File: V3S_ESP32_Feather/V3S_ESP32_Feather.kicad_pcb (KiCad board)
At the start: 4 copper layers, 30.5 x 48.3 mm, 94 parts, among them J1 USB_B_Micro, J2 Bat, J3 CAM, J4 PWM, J5 U.FL-R-SMT(01), J6 UART, J7 Micro_SD_Card_Det, J8 I2C, J9 I2C, U1 V3S, U2 MIC5504-1.2YM5, U3 MIC5501-3.0YM5, U4 ICM-20948, U5 ESP32-PICO-D4, U6 LT1963AxST-3.3, U7 BMP280, U8 MIC5504-1.8YM5, U9 MAX13030EEBET, Y1 X1E0000210832, Y2 CC5V-T1A 32.768KHZ +-20PPM 12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

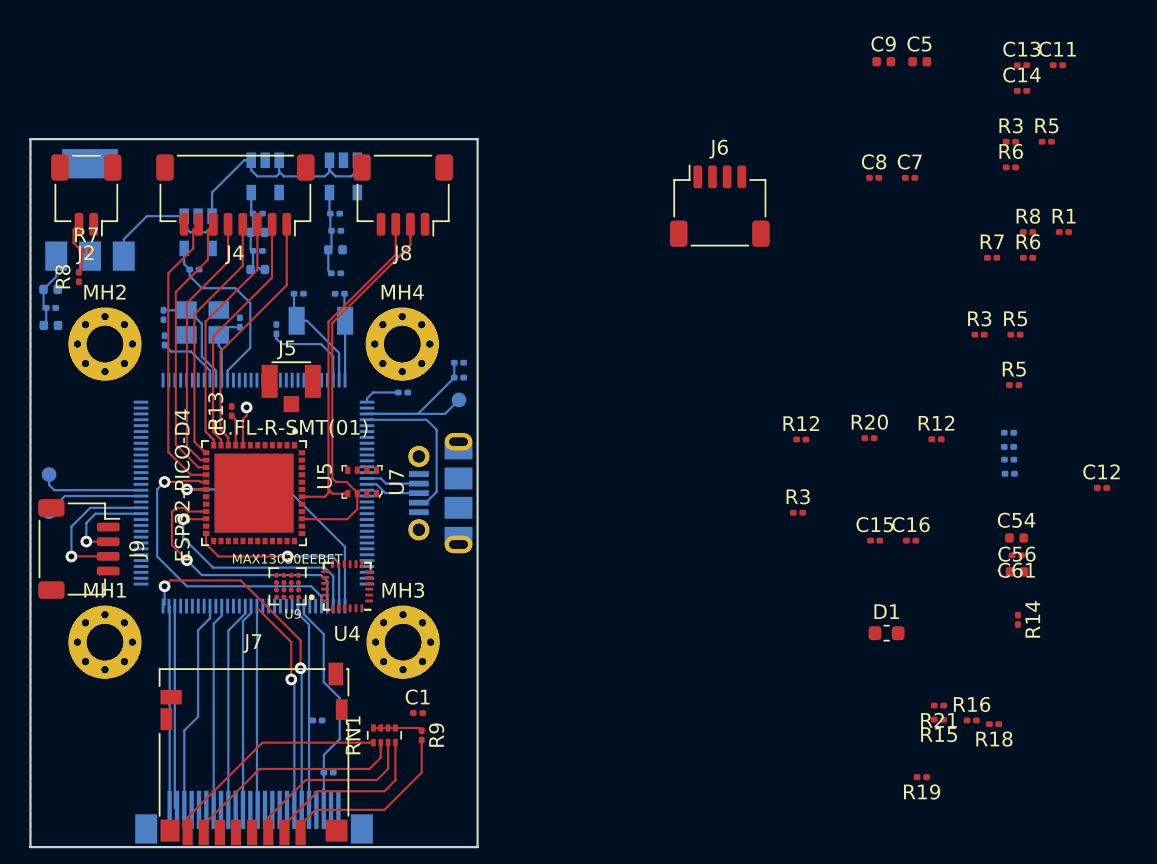
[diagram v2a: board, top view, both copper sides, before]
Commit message: Change Max13030 and moove ESP32
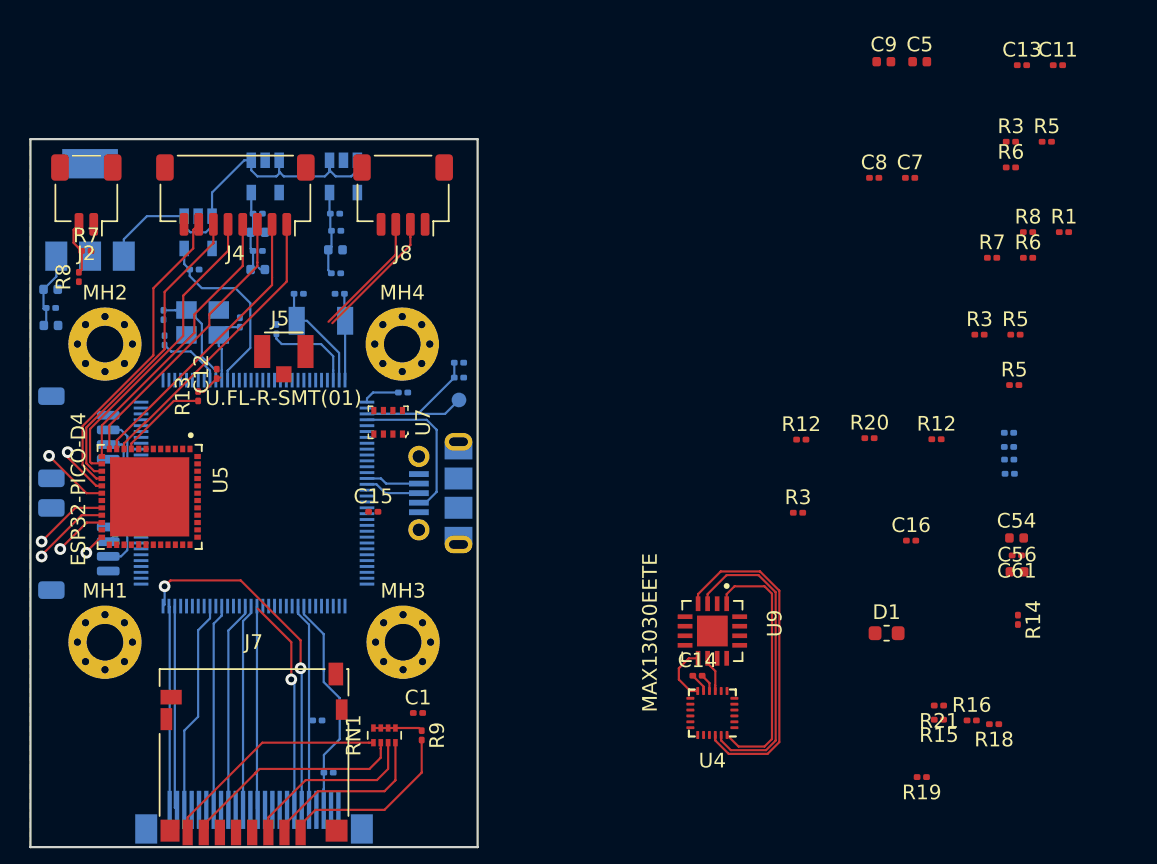
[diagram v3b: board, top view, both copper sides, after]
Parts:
- removed J6: UART, Connector_JST:JST_SH_SM04B-SRSS-TB_1x04-1MP_P1.00mm_Horizontal
- removed TP2: CPU_RX, TestPoint:TestPoint_Pad_D1.0mm
- removed TP3: CPU_TX, TestPoint:TestPoint_Pad_D1.0mm
- added J10: UART, Connector_JST:JST_SH_SM04B-SRSS-TB_1x04-1MP_P1.00mm_Horizontal, B.Cu at (26.2, 40.6)
- J9: moved to B.Cu
- U9: value MAX13030EEBET -> MAX13030EETE; footprint MAX13030EEBET:BGA16C50P4X4_202X202X67N -> MAX13035EETET:QFN65P400X400X80-17N
- moved C12 60.8 mm to (35.6, 36.3), turned to 90 degrees
- moved C14 45.6 mm to (68.3, 56.9)
- moved C15 34.3 mm to (46.2, 45.7)
- moved U9 29.1 mm to (69.3, 53.8), turned to 270 degrees
- moved U4 26.3 mm to (69.3, 59.4)
- moved U5 7.12 mm to (31.0, 44.7)
- moved U7 4.44 mm to (47.2, 39.6)
- moved R13 2.50 mm to (34.3, 37.8)
- moved J5 2.09 mm to (40.1, 34.8)
- turned J9 to 90 degrees
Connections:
- J3 pad 1: /All V3s input output/STROBE -> (no net)
- J3 pad 10: Net-(J3-Pad10) -> (no net)
- J7 pad 10: Net-(J7-Pad10) -> (no net)
- J7 pad 9: Net-(J7-Pad9) -> (no net)
- U1 pad 10: Net-(U1-Pad10) -> (no net)
- U1 pad 11: Net-(U1-Pad11) -> (no net)
- U1 pad 112: Net-(U1-Pad112) -> (no net)
- U1 pad 113: Net-(U1-Pad113) -> (no net)
- U1 pad 114: Net-(U1-Pad114) -> (no net)
- U1 pad 120: Net-(U1-Pad120) -> (no net)
- U1 pad 121: Net-(U1-Pad121) -> (no net)
- U1 pad 124: Net-(U1-Pad124) -> (no net)
- U1 pad 125: Net-(U1-Pad125) -> (no net)
- U1 pad 13: Net-(U1-Pad13) -> (no net)
- U1 pad 14: Net-(U1-Pad14) -> (no net)
- U1 pad 43: Net-(U1-Pad43) -> (no net)
- U1 pad 44: Net-(U1-Pad44) -> (no net)
- U1 pad 52: Net-(U1-Pad52) -> (no net)
- U1 pad 53: Net-(U1-Pad53) -> (no net)
- U1 pad 54: Net-(U1-Pad54) -> (no net)
- U1 pad 55: Net-(U1-Pad55) -> (no net)
- U1 pad 6: Net-(U1-Pad6) -> (no net)
- U1 pad 7: Net-(U1-Pad7) -> (no net)
- U1 pad 77: Net-(U1-Pad77) -> (no net)
- U1 pad 78: Net-(U1-Pad78) -> (no net)
- U1 pad 81: Net-(U1-Pad81) -> (no net)
- U1 pad 82: Net-(U1-Pad82) -> (no net)
- U1 pad 83: Net-(U1-Pad83) -> (no net)
- U1 pad 84: Net-(U1-Pad84) -> (no net)
- U1 pad 86: Net-(U1-Pad86) -> (no net)
- U1 pad 87: Net-(U1-Pad87) -> (no net)
- U1 pad 89: Net-(U1-Pad89) -> (no net)
- U1 pad 90: Net-(U1-Pad90) -> (no net)
- U1 pad 91: Net-(U1-Pad91) -> (no net)
- U1 pad 92: Net-(U1-Pad92) -> (no net)
- U2 pad 4: Net-(U2-Pad4) -> (no net)
- U3 pad 4: Net-(U3-Pad4) -> (no net)
- U4 pad 1: Net-(U4-Pad1) -> (no net)
- U4 pad 14: Net-(U4-Pad14) -> (no net)
- U4 pad 15: Net-(U4-Pad15) -> (no net)
- U4 pad 16: Net-(U4-Pad16) -> (no net)
- U4 pad 17: Net-(U4-Pad17) -> (no net)
- U4 pad 19: Net-(U4-Pad19) -> (no net)
- U4 pad 2: Net-(U4-Pad2) -> (no net)
- U4 pad 21: Net-(U4-Pad21) -> (no net)
- U4 pad 3: Net-(U4-Pad3) -> (no net)
- U4 pad 4: Net-(U4-Pad4) -> (no net)
- U4 pad 5: Net-(U4-Pad5) -> (no net)
- U4 pad 6: Net-(U4-Pad6) -> (no net)
- U4 pad 7: Net-(U4-Pad7) -> (no net)
- U5 pad 25: Net-(U5-Pad25) -> (no net)
- U5 pad 26: Net-(U5-Pad26) -> (no net)
- U5 pad 27: Net-(U5-Pad27) -> (no net)
- U5 pad 28: /TX -> (no net)
- U5 pad 29: /WIFI, BT, RT/SD3 -> (no net)
- U5 pad 30: Net-(U5-Pad30) -> (no net)
- U5 pad 31: Net-(U5-Pad31) -> (no net)
- U5 pad 32: Net-(U5-Pad32) -> (no net)
- U5 pad 33: Net-(U5-Pad33) -> (no net)
- U5 pad 5: Net-(U5-Pad5) -> (no net)
- U5 pad 8: /RX -> (no net)
- U8 pad 4: Net-(U8-Pad4) -> (no net)
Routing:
- net /WIFI, BT, RT/CS1.8: track 0.00 -> 23.1 mm
- net /WIFI, BT, RT/CLK1.8: track 0.00 -> 21.1 mm
- net /SDA: track 26.8 -> 8.94 mm
- net /WIFI, BT, RT/MOSI1.8: track 0.00 -> 17.7 mm
- net /All V3s input output/SDIO1_CLK: track 21.2 -> 4.20 mm
- net /SCL: track 24.3 -> 8.54 mm
- net /All V3s input output/SDIO1_DAT2: track 17.7 -> 4.65 mm
- net /All V3s input output/SDIO1_CMD: track 18.1 -> 5.32 mm
- net /All V3s input output/SDIO1_DAT0: track 16.2 -> 3.58 mm
- net /All V3s input output/SDIO1_DAT1: track 13.2 -> 1.53 mm
- net Net-(J9-Pad3): track 9.82 -> 3.76 mm, vias 1 -> 0
- net /All V3s input output/SDIO1_DAT3: track 0.00 -> 5.05 mm, vias 0 -> 1
- net Net-(R13-Pad1): track 2.12 -> 6.13 mm
- net /WIFI, BT, RT/ICM_INT1.8: track 0.00 -> 3.97 mm
- net /IO25: track 18.0 -> 20.9 mm
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
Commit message: ICM rooted
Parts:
- moved C11 59.4 mm to (39.7, 41.6), turned to 180 degrees
- moved C13 57.7 mm to (39.6, 42.7), turned to 180 degrees
- moved C16 38.9 mm to (48.5, 29.5), turned to 270 degrees
- moved R20 36.0 mm to (46.2, 28.4)
- moved U4 33.1 mm to (42.7, 39.9), turned to 0 degrees
- moved R12 30.2 mm to (47.0, 30.5), turned to 180 degrees
- moved C14 28.6 mm to (43.7, 42.4), turned to 180 degrees
- moved U9 28.0 mm to (42.7, 45.5), turned to 90 degrees
- moved C15 14.9 mm to (50.5, 31.5)
- moved U7 10.8 mm to (50.8, 29.5), turned to 90 degrees
- moved J5 3.25 mm to (42.2, 32.3)
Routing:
- net /WIFI, BT, RT/ICM_INT: track 0.00 -> 26.6 mm
- net /WIFI, BT, RT/CS: track 0.00 -> 17.6 mm
- net /WIFI, BT, RT/CLK: track 0.00 -> 14.2 mm
- net /WIFI, BT, RT/MISO: track 0.00 -> 12.0 mm, vias 0 -> 2
- net +3V3: track 8.78 -> 18.2 mm, vias 0 -> 1
- net /WIFI, BT, RT/MOSI: track 0.00 -> 8.42 mm, vias 0 -> 2
- net /SCL: track 8.54 -> 15.4 mm, vias 0 -> 1
- net +1V8: track 5.68 -> 9.41 mm
- net /SDA: track 8.94 -> 11.1 mm, vias 0 -> 1
- net GND: vias 0 -> 1

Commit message: Camera routed
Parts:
- removed the R12 at (84.6, 40.8)
- removed the R3 at (89.7, 20.5)
- removed the R3 at (87.6, 33.6)
- removed the R5 at (90.0, 33.6)
- removed the R5 at (89.9, 37.1)
- removed the R6 at (90.9, 28.4)
- removed the R7 at (88.4, 28.4)
- removed the R8 at (90.9, 26.7)
- C5, C9, R1, R15, R16, R18, R19, R21, R3, R5, R6: moved to B.Cu
- moved R5 70.1 mm to (29.1, 51.2), turned to 90 degrees
- moved C7 66.1 mm to (30.0, 62.7), turned to 180 degrees
- moved R6 65.1 mm to (28.4, 44.5), turned to 90 degrees
- moved C8 64.8 mm to (30.0, 63.8), turned to 180 degrees
- moved R14 64.7 mm to (25.5, 49.8)
- moved C64 61.1 mm to (29.7, 31.1)
- moved R31 61.0 mm to (29.7, 30.2)
- moved C9 60.1 mm to (24.1, 34.3)
- moved R32 59.6 mm to (31.0, 30.5), turned to 270 degrees
- moved C65 58.5 mm to (31.9, 30.5), turned to 270 degrees
- moved D1 58.3 mm to (28.4, 29.2)
- moved C5 53.7 mm to (31.5, 28.4), turned to 270 degrees
- moved R1 46.8 mm to (48.3, 39.5)
- moved R16 42.8 mm to (44.6, 54.4), turned to 270 degrees
- moved R21 42.2 mm to (42.8, 54.4), turned to 270 degrees
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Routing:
- net /All V3s input output/SDIO1_DAT2: track 4.65 -> 38.4 mm, vias 1 -> 2
- net /All V3s input output/SDIO1_DAT3: track 5.05 -> 34.0 mm, vias 1 -> 2
- net /All V3s input output/SDIO1_DAT0: track 3.58 -> 29.9 mm, vias 1 -> 2
- net /All V3s input output/SDIO1_CMD: track 5.32 -> 31.1 mm, vias 1 -> 2
- net /All V3s input output/SDIO1_DAT1: track 1.53 -> 26.4 mm, vias 1 -> 2
- net /All V3s input output/SDIO1_CLK: track 4.20 -> 27.7 mm, vias 1 -> 2
- net /WIFI, BT, RT/ICM_INT: track 26.6 -> 3.59 mm, vias 0 -> 1
- net /All V3s input output/CSI_HSYNC: track 0.00 -> 22.4 mm, vias 0 -> 2
- net /All V3s input output/CSI_PCLK: track 0.00 -> 21.6 mm, vias 0 -> 2
- net /All V3s input output/CSI_MCLK: track 0.00 -> 21.0 mm, vias 0 -> 2
- net /All V3s input output/CSI_PWDN: track 0.00 -> 20.9 mm, vias 0 -> 2
- net /All V3s input output/CSI_Y5: track 0.00 -> 16.1 mm
- net /All V3s input output/CSI_Y2: track 0.00 -> 15.2 mm, vias 0 -> 2
- net /All V3s input output/CSI_Y3: track 0.00 -> 14.3 mm, vias 0 -> 2
- net /PMIC Power Battery/SVREF: track 0.00 -> 11.1 mm
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- added copper zone on In1.Cu, net GND
- added copper zone on In2.Cu, net GND

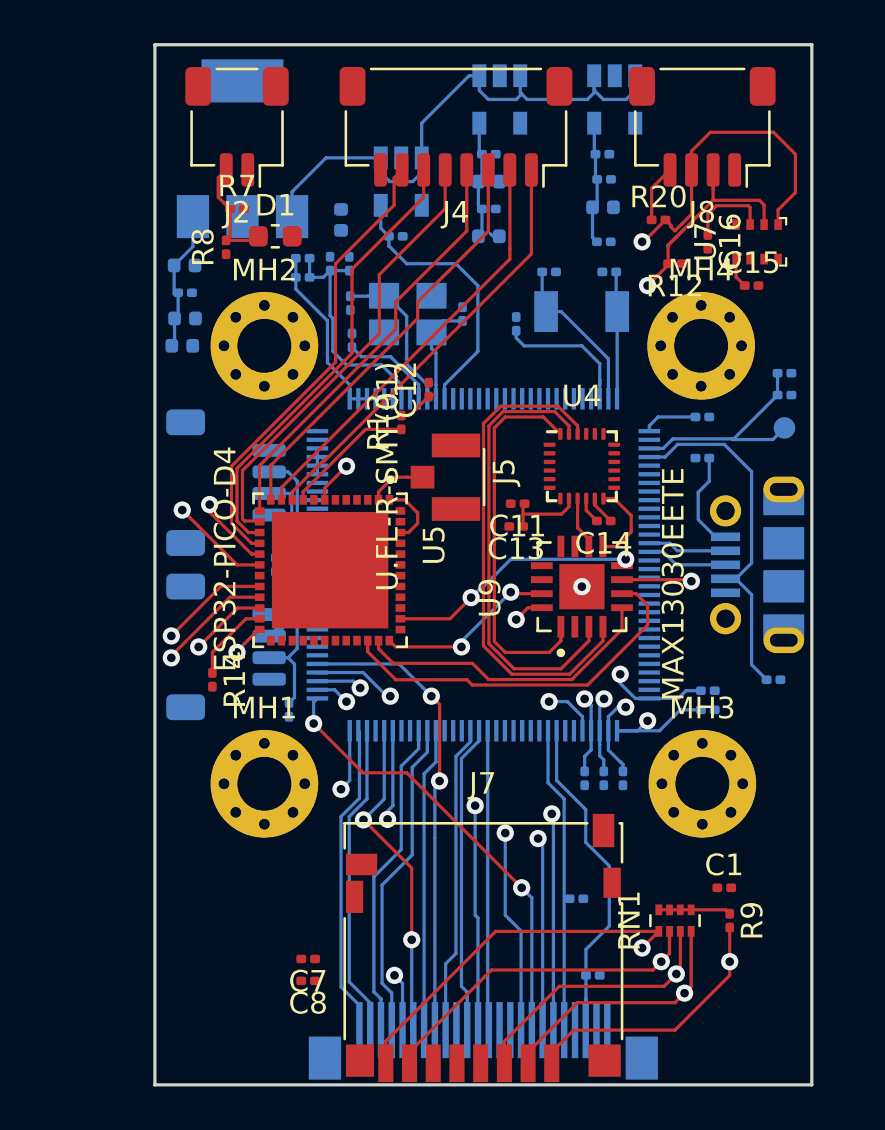
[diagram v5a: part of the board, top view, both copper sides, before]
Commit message: Sdcard part routed
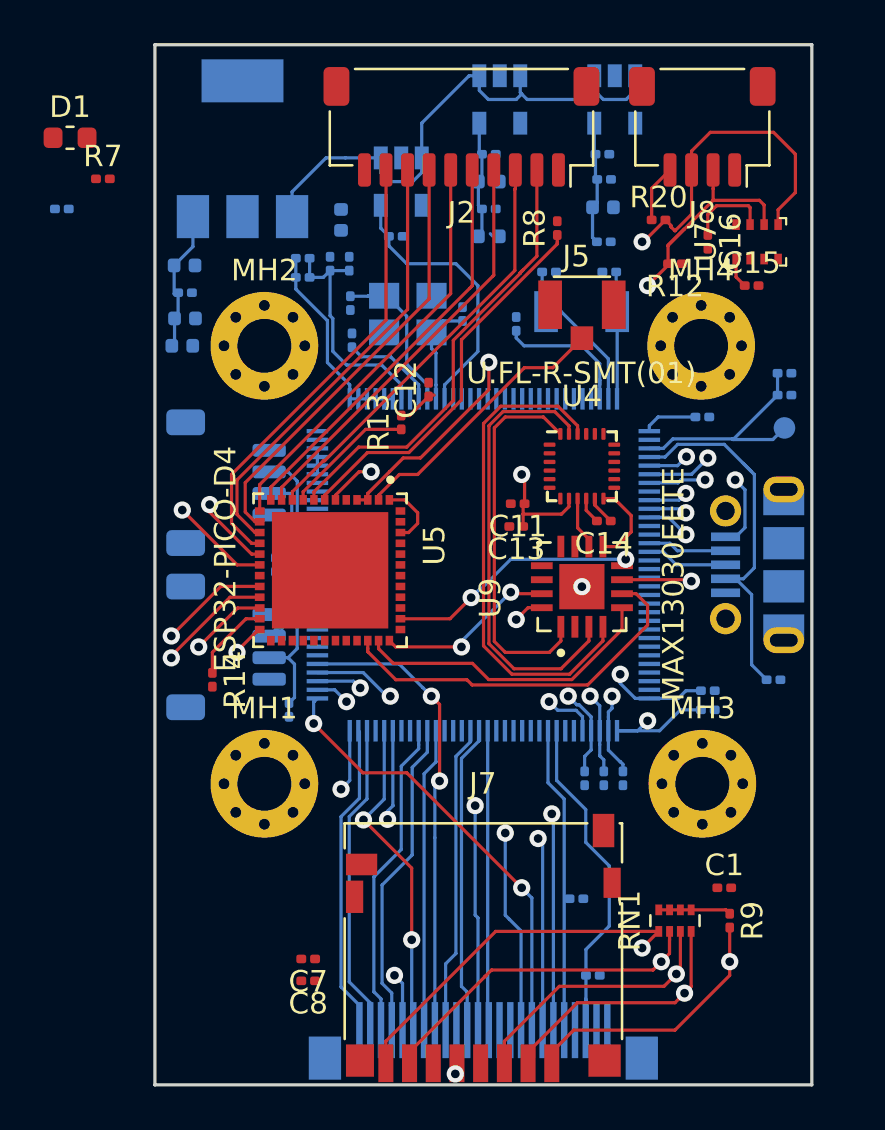
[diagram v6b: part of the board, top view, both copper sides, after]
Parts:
- removed J4: PWM, Connector_JST:JST_SH_SM08B-SRSS-TB_1x08-1MP_P1.00mm_Horizontal
- J2: value Bat -> PWM; footprint Connector_JST:JST_SH_SM02B-SRSS-TB_1x02-1MP_P1.00mm_Horizontal -> Connector_JST:JST_SH_SM10B-SRSS-TB_1x10-1MP_P1.00mm_Horizontal
- moved R1 31.9 mm to (18.5, 27.9)
- moved R8 15.4 mm to (41.5, 28.8)
- moved D1 10.6 mm to (18.9, 24.6)
- moved J2 10.4 mm to (37.1, 24.1)
- moved J5 9.91 mm to (42.7, 32.4), turned to 0 degrees
- moved R7 6.38 mm to (20.4, 26.5)
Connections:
- J2 pad 1: GND -> +BATT
- J2 pad 2: +BATT -> /SENSOR_VN
- U5 pad 8: (no net) -> /SENSOR_VN
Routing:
- net /All V3s input output/PF3: track 12.3 -> 52.1 mm, vias 1 -> 2
- net /All V3s input output/PF4: track 11.9 -> 47.9 mm, vias 1 -> 2
- net /All V3s input output/PF2: track 0.00 -> 35.8 mm, vias 0 -> 2
- net /All V3s input output/PF5: track 12.5 -> 41.8 mm, vias 1 -> 2
- net /All V3s input output/PF1: track 15.6 -> 43.1 mm, vias 1 -> 2
- net /All V3s input output/PF0: track 16.9 -> 43.9 mm, vias 1 -> 2
- net /SENSOR_VN: track 0.00 -> 21.1 mm
- net Net-(R8-Pad1): track 1.98 -> 17.9 mm, vias 1 -> 0
- net Net-(J5-Pad3): track 2.70 -> 12.7 mm
- net +3V3: track 22.5 -> 32.2 mm, vias 1 -> 2
- net +BATT: track 31.8 -> 26.5 mm
- net /WIFI, BT, RT/ICM_INT: track 3.59 -> 5.92 mm, vias 1 -> 2
- net +1V8: track 20.2 -> 21.6 mm, vias 0 -> 1
- net /USB_ID: track 16.5 -> 17.9 mm
- net /All V3s input output/SDIO1_DAT0: track 29.9 -> 29.0 mm
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
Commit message: last 4 layers version
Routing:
- net /WIFI, BT, RT/UART0_TX: track 0.00 -> 10.9 mm, vias 0 -> 1
- net /WIFI, BT, RT/UART0_RX: track 0.00 -> 9.45 mm, vias 0 -> 1
- net /WIFI, BT, RT/IO2_PULL: track 0.00 -> 7.74 mm, vias 0 -> 2
- net +3V3: track 32.2 -> 38.6 mm
- net /SCL: track 15.4 -> 18.4 mm, vias 1 -> 2
- net +1V8: track 21.6 -> 23.4 mm, vias 1 -> 3
- net /All V3s input output/SDIO1_DAT3: track 34.0 -> 34.9 mm
